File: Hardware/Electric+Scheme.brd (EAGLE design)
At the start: 170.2 x 111.4 mm, 103 parts, among them IC1 BD5229G-TR, IC4 XC6220A331MR-G, J1 FH34SRJ-24S-0.5SH_99_, J2 SAMACSYS_PARTS_USB4110-GF-A, J3 QWIIC_RIGHT_ANGLE, J4 112A-TAAR-R03_ATTEND, Q1 20V/4.2A/52mΩ/1.4W, Q2 20V/4.2A/52mΩ/1.4W, Q3 SI1308EDL-T1-GE3, U1 W25Q512JVEIQ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

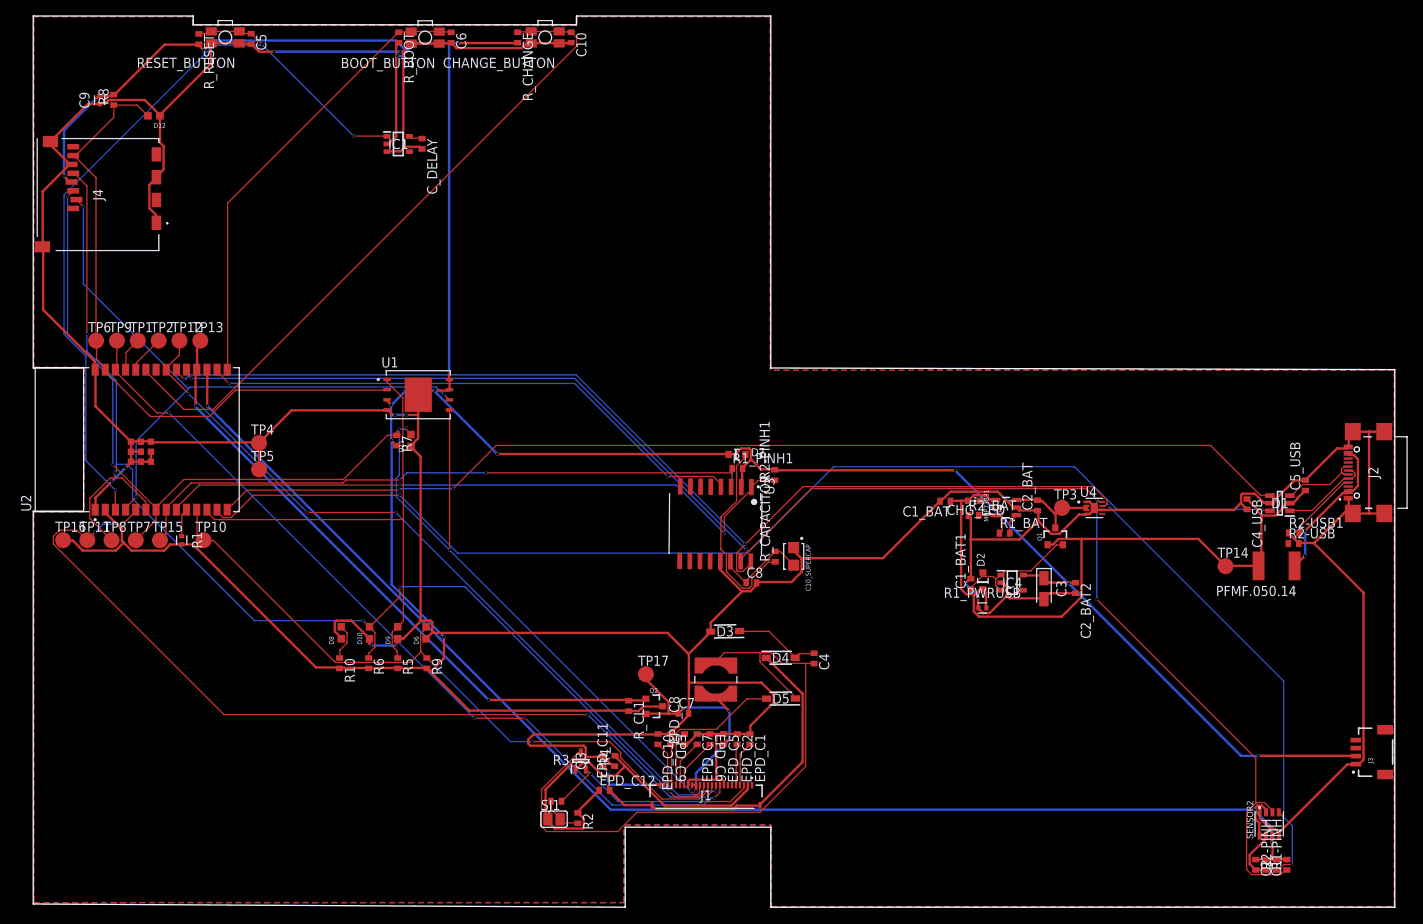
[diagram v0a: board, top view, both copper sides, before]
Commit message: Add files via upload
Updated pcb, rerouted and moved labels.
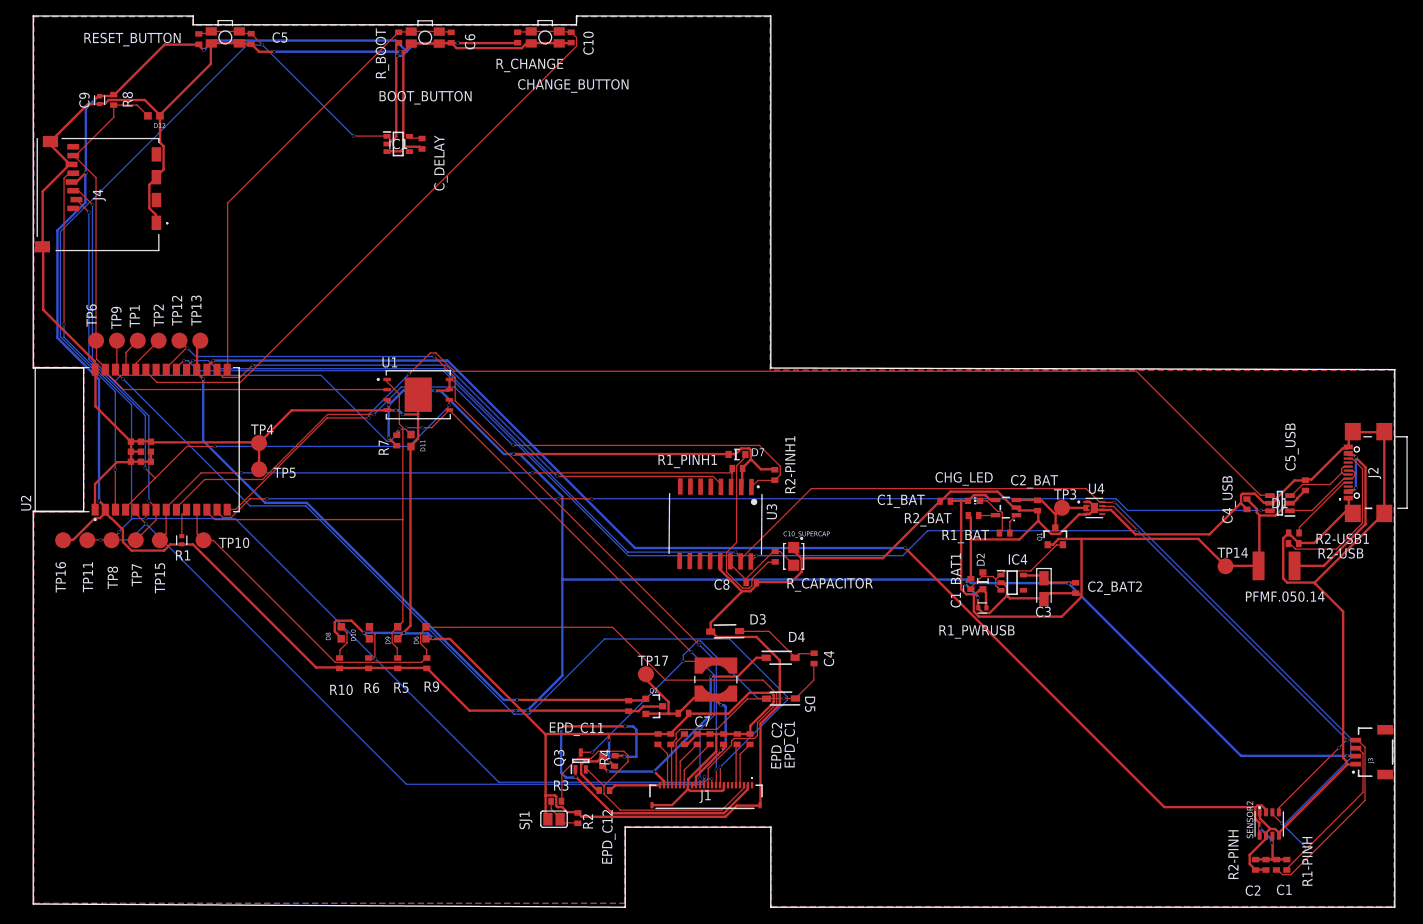
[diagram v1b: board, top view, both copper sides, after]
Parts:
- CHG_LED: value (none) -> RED
- SJ1: value (none) -> SOLDERJUMPER
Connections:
- removed net N$7: J3.4
- new net N$15: EPD_C12.2, J1.24
- net GND: now also J1.MP1, J1.MP2
- net N$4: now also J2.B5, R2-USB.1; no longer J3.3
- net PREVGL: no longer EPD_C12.2, J1.24, J1.MP1, J1.MP2
- net SCL: now also J3.4
- net SDA: now also J3.3
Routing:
- net GND: track 631.1 -> 673.4 mm, vias 10 -> 11
- net SRC: track 81.9 -> 45.4 mm, vias 0 -> 3
- net 3V3: track 412.1 -> 439.7 mm
- net EPD_BUSY: track 103.5 -> 127.1 mm, vias 4 -> 2
- net PREVGL: track 53.1 -> 31.6 mm
- net GDR: track 28.3 -> 49.5 mm, vias 0 -> 4
- net SDA: track 193.0 -> 214.2 mm, vias 4 -> 5
- net EPD_CS: track 86.6 -> 106.9 mm, vias 2 -> 0
- net N$4: track 0.00 -> 20.0 mm
- net SCL: track 194.8 -> 213.0 mm
- net SCK: track 160.4 -> 144.4 mm
- net RESE: track 27.5 -> 42.1 mm, vias 2 -> 0
- net EPD_DC: track 110.3 -> 95.8 mm, vias 4 -> 3
- net USB_D+: track 136.3 -> 146.1 mm
- net USB_D-: track 143.1 -> 133.8 mm, vias 2 -> 4
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
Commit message: Update plan de masa.
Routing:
- net GND: vias 11 -> 29
